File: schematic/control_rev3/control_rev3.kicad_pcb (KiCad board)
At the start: 2 copper layers, 48.3 x 105.4 mm, 126 parts, among them J28 Conn_02x07, J29 Conn_02x07, J30 Conn_01x16, J31 Conn_01x16, J32 Conn_02x05_Odd_Even, J33 MIDI, J34 Conn_02x02_Odd_Even, J38 QWIIC, Q1 FDV303N, Q2 FDV303N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

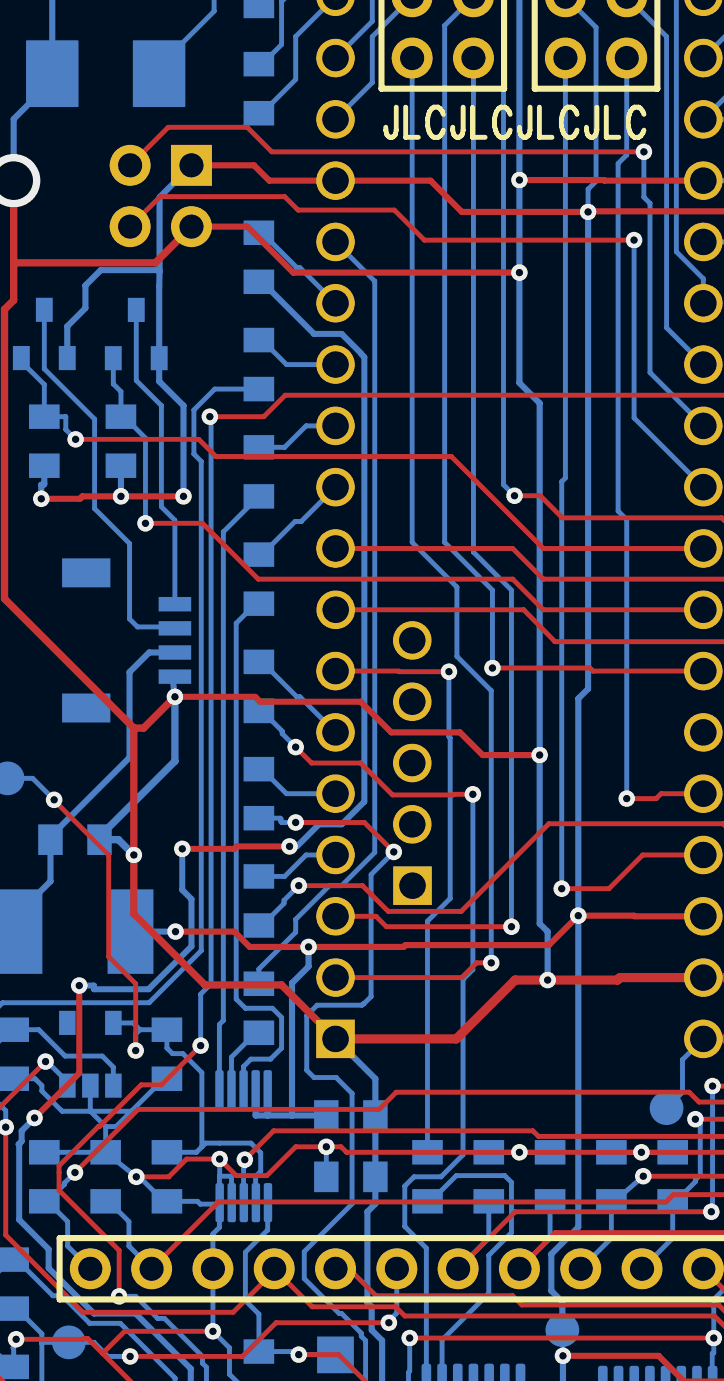
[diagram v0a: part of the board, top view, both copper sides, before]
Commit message: added D6 per Paul's recommendation, to help protect U17
reduced pads on ADC footprint to help prevent solder bridging

updated a few footprint silkscreens to look more like original rev3 board

generated updated gerber zip files

TODO: update IC pads to match more closely to original rev3 board if it makes soldering easier
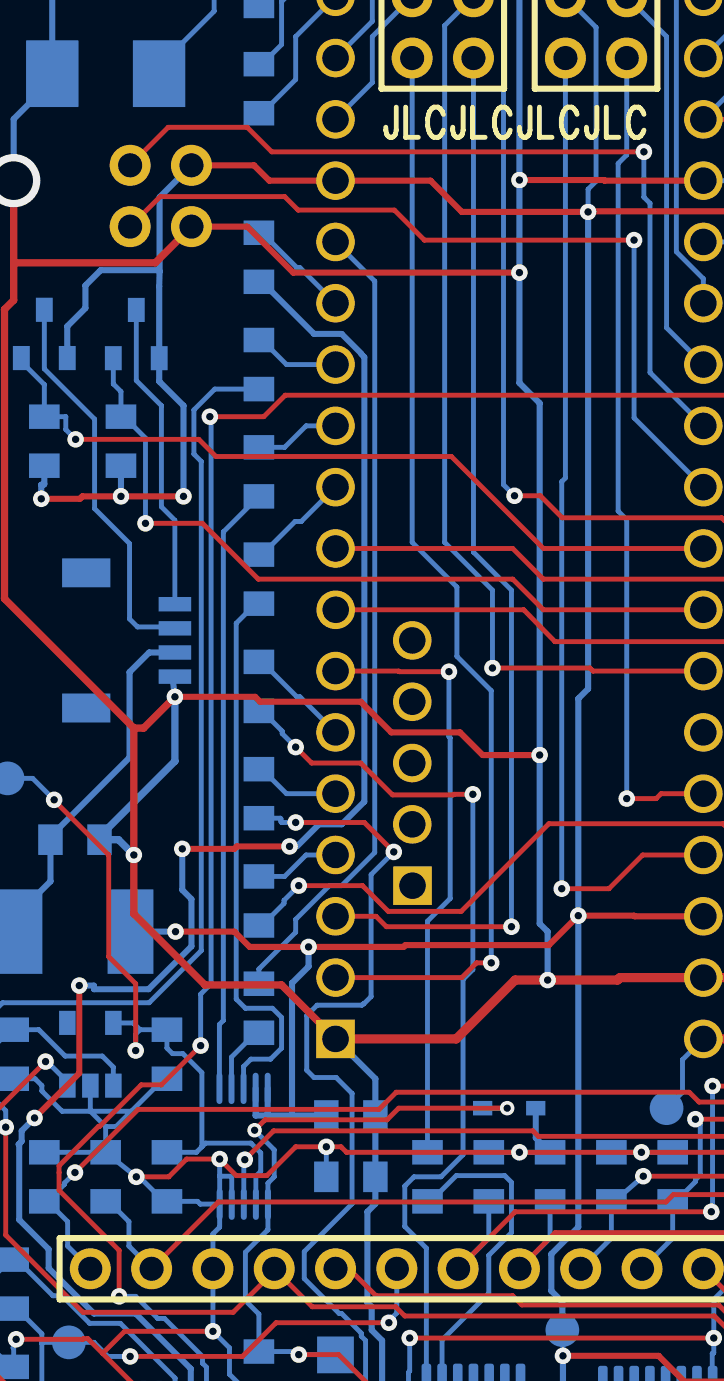
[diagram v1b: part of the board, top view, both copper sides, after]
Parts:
- added D6: BZT52B5V1S, Custom_Footprints:D_SOD-323F_rectpads, B.Cu at (47.8, 93.0)
- J32: footprint Connector_IDC:IDC-Header_2x05_P2.54mm_Vertical -> Custom_Footprints:IDC-Header_2x05_P2.54mm_Vertical_reduced
- J34: footprint Connector_PinHeader_2.54mm:PinHeader_2x02_P2.54mm_Vertical -> Custom_Footprints:PinHeader_2x02_P2.54mm_Vertical_symmetric
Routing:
- net Net-(D6-K): track 35.9 -> 51.3 mm, vias 2 -> 4
- net GND: track 493.2 -> 495.5 mm
